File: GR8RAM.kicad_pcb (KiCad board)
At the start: 4 copper layers, 107.6 x 59.8 mm, 46 parts, among them J1 AppleIIBus, J2 JTAG, U1 EPM7128SL84, U2 512Kx8 Flash, U3 4Mx4 DRAM, U4 4Mx4 DRAM, U5 4Mx4 DRAM, U6 4Mx4 DRAM

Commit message: Board done?
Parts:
- removed JP1: Mode, Connector_PinHeader_2.54mm:PinHeader_1x02_P2.54mm_Vertical_SMD_Pin1Left
- added C23: 2u2, stdpads:C_0603, F.Cu at (103.8, 104.3)
- added C24: 2u2, stdpads:C_0603, F.Cu at (103.8, 100.9)
- added C25: 2u2, stdpads:C_0603, F.Cu at (97.2, 91.7)
- added C26: 2u2, stdpads:C_0603, F.Cu at (90.2, 91.7)
- added C27: 2u2, stdpads:C_0603, F.Cu at (106.0, 98.8)
- added C28: 2u2, stdpads:C_0603, F.Cu at (123.7, 115.3)
- added C29: 2u2, stdpads:C_0603, F.Cu at (126.5, 112.6)
- added C30: 2u2, stdpads:C_0603, F.Cu at (126.5, 107.8)
- added C31: 2u2, stdpads:C_0603, F.Cu at (126.5, 103.8)
- added C32: 2u2, stdpads:C_0603, F.Cu at (126.5, 93.4)
- added C33: 2u2, stdpads:C_0603, F.Cu at (110.8, 104.0)
- added C34: 2u2, stdpads:C_0603, F.Cu at (110.8, 108.7)
- added C35: 2u2, stdpads:C_0603, F.Cu at (113.7, 115.3)
- added C36: 10u, stdpads:C_0805, F.Cu at (131.7, 98.5)
- added C37: 10u, stdpads:C_0805, F.Cu at (131.7, 101.0)
- added C38: 22n, stdpads:R_0805, F.Cu at (129.5, 110.8)
- added D1: SS14, stdpads:D_SMA, F.Cu at (141.9, 100.0)
- added D2: SMBJ5.0A, stdpads:D_SMB, F.Cu at (137.3, 100.0)
- added D3: SS14, stdpads:D_SMA, F.Cu at (141.9, 112.7)
- added F1: nSMD035-16V, stdpads:BelFuse_1206, F.Cu at (135.4, 93.5)
- added FB1: GZ2012D601TF, stdpads:Murata_BLM21, F.Cu at (139.5, 95.5)
- added H6: , stdpads:PasteHole_1.152mm_NPTH, F.Cu at (143.0, 127.0)
- added J3: DC in, stdpads:BOOMELE_DC-005_DC_5.5-2.0MM, F.Cu at (102.8, 86.5)
- added J4: JTAG, Connector_IDC:IDC-Header_2x05_P2.54mm_Vertical, F.Cu at (64.1, 108.2)
- added Q1: AO3401A, stdpads:SOT-23, F.Cu at (141.9, 118.2)
- added R10: 1k, stdpads:R_0805, F.Cu at (132.9, 113.2)
- added R11: 1k, stdpads:R_0805, F.Cu at (138.3, 118.1)
- added R12: 1k, stdpads:R_0805, F.Cu at (139.5, 91.5)
- added R13: 100, stdpads:R_0805, F.Cu at (139.5, 93.5)
- added R14: 0, stdpads:R_0805, F.Cu at (129.8, 119.9)
- added R6: 1k, stdpads:R_0805, F.Cu at (137.1, 111.9)
- added R7: 1k, stdpads:R_0805, F.Cu at (136.1, 123.0)
- added R8: 1M, stdpads:R_0805, F.Cu at (132.9, 111.2)
- added R9: 3k3, stdpads:R_0805, F.Cu at (138.3, 114.7)
- added RN1: 4x33, stdpads:R4_0402, F.Cu at (108.2, 95.2)
- added RN2: 4x33, stdpads:R4_0402, F.Cu at (108.5, 106.2)
- added RN3: 4x33, stdpads:R4_0402, F.Cu at (108.5, 110.7)
- added RN4: 4x10k, stdpads:R4_0402, F.Cu at (128.8, 124.0)
- added U12: 74AHCT125, stdpads:TSSOP-14_4.4x5mm_P0.65mm, F.Cu at (117.0, 122.0)
- added U13: 25M, stdpads:Crystal_SMD_3225-4Pin_3.2x2.5mm, F.Cu at (107.1, 102.5)
- added U14: 74AHCT125, stdpads:TSSOP-14_4.4x5mm_P0.65mm, F.Cu at (124.5, 122.0)
- added U16: 74LVC1G04GW, stdpads:SOT-353, F.Cu at (108.2, 98.8)
- added U7: LM393, stdpads:SOIC-8_3.9mm, F.Cu at (134.5, 118.0)
- added U8: AP2125, stdpads:SOT-23, F.Cu at (138.3, 106.5)
- added U9: 74AHC245, stdpads:TSSOP-20_4.4x6.5mm_P0.65mm, F.Cu at (99.4, 122.0)
- C1, C10, C11, C2, C3, C4, C5, C6, C7, C8: value 2u2 -> 10u
- C12, C13, C17, C18, C19, C20, C21, C22, C9: footprint stdpads:C_0805 -> stdpads:C_0603
- C14, C15, C16: value DNP -> 2u2; footprint stdpads:CP_EIA-3528 -> stdpads:C_0603
- H2, H3, H4, H5: footprint stdpads:PasteHole_1.1mm_PTH -> stdpads:PasteHole_1.152mm_NPTH
- J2: footprint stdpads:IDC_SMD_2x05_P2.54mm_Vertical -> Connector:Tag-Connect_TC2050-IDC-FP_2x05_P1.27mm_Vertical
- R1, R2: value 100 -> DNP
- R3: value 100 -> 2k7
- R4: value 15 -> 2k2
- R5: value 22k -> 1M
- U1: value EPM7128SL84 -> EPM240T100C5N; footprint stdpads:PLCC-84_SMDSocket -> stdpads:TQFP-100_14x14mm_P0.5mm
- U2: value 512Kx8 Flash -> W9825; footprint stdpads:PLCC-32_SMDSocket -> stdpads:TSOP-II-54_22.2x10.16mm_P0.8mm
- U3: value 4Mx4 DRAM -> MX29LV640EB; footprint stdpads:SOP-24-26-300mil -> stdpads:TSOP-I-48_18.4x12mm_P0.5mm
- U4, U5, U6: value 4Mx4 DRAM -> 74AHC245; footprint stdpads:SOP-24-26-300mil -> stdpads:TSSOP-20_4.4x6.5mm_P0.65mm
- moved H5 108.2 mm to (140.5, 82.4), turned to 270 degrees
- moved H4 93.0 mm to (58.3, 86.0), turned to 90 degrees
- moved J2 76.6 mm to (63.9, 119.3)
- moved C8 74.4 mm to (142.6, 106.5)
- moved C3 71.3 mm to (116.2, 128.3), turned to 0 degrees
- moved U2 68.4 mm to (118.7, 103.0), turned to 180 degrees
- moved C1 65.6 mm to (136.3, 128.3)
- moved C13 60.3 mm to (76.6, 119.8), turned to 270 degrees
- moved C7 56.8 mm to (142.6, 104.5), turned to 0 degrees
- moved C16 56.0 mm to (104.2, 119.8), turned to 270 degrees
- moved C14 54.8 mm to (85.8, 119.8), turned to 270 degrees
- moved C15 53.7 mm to (95.0, 119.8), turned to 270 degrees
- moved C10 50.8 mm to (134.8, 106.5), turned to 90 degrees
- moved H1 47.1 mm to (140.5, 129.5), turned to 0 degrees
- moved R5 46.1 mm to (132.7, 123.0), turned to 0 degrees
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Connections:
- C10 pad 1: +5V -> +3V3
- C11 pad 1: +5V -> +3V3
- C12 pad 1: +5V -> +3V3
- C13 pad 1: +5V -> +3V3
- C14 pad 1: +5V -> +3V3
- C15 pad 1: +5V -> +3V3
- C16 pad 1: +5V -> +3V3
- C17 pad 1: GND -> +5V
- C17 pad 2: -5V -> GND
- C18 pad 1: +5V -> +3V3
- C18 pad 2: -5V -> GND
- C19 pad 1: +12V -> +3V3
- C2 pad 1: +5V -> GND
- C2 pad 2: GND -> -12V
- C20 pad 1: GND -> +3V3
- C20 pad 2: -12V -> GND
- C21 pad 1: +5V -> +3V3
- C21 pad 2: +12V -> GND
- C22 pad 1: -12V -> +3V3
- C22 pad 2: -5V -> GND
- C3 pad 1: +5V -> GND
- C3 pad 2: GND -> -5V
- C4 pad 1: +5V -> +12V
- C5 pad 1: +5V -> VBUS
- C6 pad 1: +5V -> Net-(C6-Pad1)
- C7 pad 1: +5V -> Vin
- C8 pad 1: +5V -> Vin
- J1 pad 22: /DMA -> /~DMA~
- J1 pad 23: /INTin -> /INTout
- J1 pad 24: /DMAin -> /DMAout
- J2 pad 4: +5V -> +3V3
- R1 pad 1: /PHI0r -> /DMAout
- R1 pad 2: /PHI0 -> /DMAin
- R2 pad 1: /PHI1r -> /INTout
- R2 pad 2: /PHI1 -> /INTin
- R3 pad 1: /Q3r -> +5V
- R3 pad 2: /Q3 -> Net-(R3-Pad2)
- R4 pad 1: /7Mr -> +3V3
- R4 pad 2: /7M -> Net-(C38-Pad1)
- R5 pad 1: +5V -> /~RES~i
- R5 pad 2: /~MODE~ -> Net-(R3-Pad2)
- U1 pad 1: /~RES~ -> /RA9
- U1 pad 10: /A9 -> GND
- U1 pad 11: /A10 -> GND
- U1 pad 12: /A11 -> /RD6
- U1 pad 13: +5V -> +3V3
- U1 pad 14: /TDI -> /RD7
- U1 pad 15: /A12 -> /RB6
- U1 pad 16: /A13 -> /RA0
- U1 pad 17: /A14 -> /D~OE~
- U1 pad 18: /A15 -> /Ddir
- U1 pad 19: GND -> /Adir
- U1 pad 2: /PHI1r -> /RD0
- U1 pad 20: /R~W~ -> /RDMAout
- U1 pad 21: /~DEVSEL~ -> /RINTout
- U1 pad 22: /~INH~ -> /TMS
- U1 pad 23: /TMS -> /TDI
- U1 pad 24: /~IOSTRB~ -> /TCK
- U1 pad 25: /D7 -> /TDO
- U1 pad 26: +5V -> /NMI~OE~
- U1 pad 27: /D6 -> /RW~OE~
- U1 pad 28: /D5 -> /RR~W~out
- U1 pad 29: /D4 -> /IRQ~OE~
- U1 pad 3: +5V -> /RA10
- U1 pad 30: /PHI1out -> /DMA~OE~
- U1 pad 31: /C7Mout -> +3V3
- U1 pad 33: /D3 -> /INH~OE~
- U1 pad 34: /D2 -> /RA11
- U1 pad 35: /D1 -> /RA12
- U1 pad 36: /D0 -> /RA13
- U1 pad 37: Net-(U1-Pad37) -> /RA14
- U1 pad 38: +5V -> /RA15
- U1 pad 39: /~CAS~0 -> /R~IOSEL~
- U1 pad 4: /A6 -> /RD1
- U1 pad 40: /~CAS~1 -> /R~DEVSEL~
- U1 pad 41: /R~CS~ -> /RPHI1
- U1 pad 42: GND -> /R~IOSTRB~
- U1 pad 43: +5V -> /RR~W~in
- U1 pad 44: /~MODE~ -> /R~RES~
- U1 pad 45: /R~OE~ -> +3V3
- U1 pad 46: /RA9 -> GND
- U1 pad 47: GND -> /Dr1
- U1 pad 48: /RA10 -> /RINTin
- U1 pad 49: /RA3 -> /RDMAin
- U1 pad 5: /A7 -> /RD2
- U1 pad 50: /RA2 -> /Dr0
- U1 pad 51: /RA5 -> /Dr4
- U1 pad 52: /RA0 -> /Dr5
- U1 pad 53: +5V -> /Dr6
- U1 pad 54: /RA1 -> /Dr7
- U1 pad 55: /RA4 -> /Dr3
- U1 pad 56: /RA7 -> /Dr2
- U1 pad 57: /RA6 -> /SDQMH
- U1 pad 58: /RA8 -> /S~WE~
- U1 pad 59: GND -> +3V3
- U1 pad 6: /Q3r -> /RD3
- U1 pad 60: /~RAS~ -> GND
- U1 pad 61: /RD7 -> /S~CAS~
- U1 pad 62: /TCK -> /S~RAS~
- U1 pad 63: /RD5 -> +3V3
- U1 pad 64: /RD6 -> /ACLK
- U1 pad 65: /RD4 -> GND
- U1 pad 66: +5V -> /SCKE
- U1 pad 67: /R~WE~ -> /S~CS~
- U1 pad 68: /RD3 -> /RB5
- U1 pad 69: /RD2 -> /RB4
- U1 pad 7: GND -> /RD4
- U1 pad 70: /RD1 -> /RB3
- U1 pad 71: /TDO -> /RB2
- U1 pad 72: GND -> /RB1
- U1 pad 73: /RD0 -> /RB0
- U1 pad 74: /~IOSEL~ -> /RB9
- U1 pad 75: /A0 -> /SA0
- U1 pad 76: /A1 -> /SA4
- U1 pad 77: /A2 -> /SA6
- U1 pad 78: +5V -> /RB10
- U1 pad 79: /A3 -> GND
- U1 pad 8: /PHI0r -> /RD5
- U1 pad 80: /A4 -> +3V3
- U1 pad 81: /A5 -> /RB11
- U1 pad 82: GND -> /RB8
- U1 pad 83: /7Mr -> /RB7
- U1 pad 84: /7Mr -> /SA3
- U1 pad 9: /A8 -> +3V3
- U2 pad 1: /RA7 -> +3V3
- U2 pad 10: /A2 -> /SD5
- U2 pad 11: /A1 -> /SD6
- U2 pad 12: /A0 -> GND
- U2 pad 13: /RD0 -> /SD7
- U2 pad 14: /RD1 -> +3V3
- U2 pad 15: /RD2 -> /SDQML
- U2 pad 16: GND -> /S~WE~
- U2 pad 17: /RD3 -> /S~CAS~
- U2 pad 18: /RD4 -> /S~RAS~
- U2 pad 19: /RD5 -> /S~CS~
- U2 pad 2: /RA5 -> /SD0
- U2 pad 20: /RD6 -> /RB4
- U2 pad 21: /RD7 -> /RB2
- U2 pad 22: /R~CS~ -> /RB0
- U2 pad 23: /A10 -> /SA0
- U2 pad 24: /R~OE~ -> /RB11
- U2 pad 25: /RA0 -> /RB8
- U2 pad 26: /A9 -> /SA3
- U2 pad 27: /A8 -> +3V3
- U2 pad 28: /RA2 -> GND
- U2 pad 29: /RA3 -> /SA4
- U2 pad 3: /RA4 -> +3V3
- U2 pad 30: /RA6 -> /RB7
- U2 pad 31: /R~WE~ -> /SA6
- U2 pad 32: +5V -> /RB10
- U2 pad 4: /RA1 -> /SD1
- U2 pad 5: /A7 -> /SD2
- U2 pad 6: /A6 -> GND
- U2 pad 7: /A5 -> /SD3
- U2 pad 8: /A4 -> /SD4
- U2 pad 9: /A3 -> +3V3
- U3 pad 1: +5V -> /RB5
- U3 pad 10: /RA2 -> /RB10
- U3 pad 11: /RA3 -> /R~WE~
- U3 pad 12: /RA10 -> +3V3
- U3 pad 13: +5V -> /RB11
- U3 pad 14: GND -> +3V3
- U3 pad 15: /RA9 -> Net-(U3-Pad15)
- U3 pad 16: /RA8 -> /RB8
- U3 pad 17: /RA6 -> /RB7
- U3 pad 18: /RA7 -> /RA8
- U3 pad 19: /RA4 -> /RA7
- U3 pad 2: /RD1 -> /RB4
- U3 pad 21: /RA1 -> /RA5
- U3 pad 22: GND -> /RA4
- U3 pad 23: /~CAS~0 -> /RA3
- U3 pad 24: /RD2 -> /RA2
- U3 pad 25: /RD0 -> /RA1
- U3 pad 26: GND -> /R~CS~
- U3 pad 3: /RD3 -> /RB3
- U3 pad 4: /R~WE~ -> /RB2
- U3 pad 5: /~RAS~ -> /RB1
- U3 pad 6: (no net) -> /RB0
- U3 pad 8: /RA0 -> /RA9
- U3 pad 9: /RA5 -> /RB9
- U4 pad 1: +5V -> /Adir
- U4 pad 10: /RA2 -> GND
- U4 pad 11: /RA5 -> /RA7
- U4 pad 12: /RA0 -> /RA6
- U4 pad 13: +5V -> /RA5
- U4 pad 14: GND -> /RA4
- U4 pad 15: /RA1 -> /RA3
- U4 pad 16: /RA4 -> /RA2
- U4 pad 17: /RA7 -> /RA1
- U4 pad 18: /RA6 -> /RA0
- U4 pad 19: /RA8 -> /A~OE~
- U4 pad 2: /RD6 -> /A0
- U4 pad 3: /RD7 -> /A1
- U4 pad 4: /R~WE~ -> /A2
- U4 pad 5: /~RAS~ -> /A3
- U4 pad 6: (no net) -> /A4
- U4 pad 8: /RA10 -> /A6
- U4 pad 9: /RA3 -> /A7
- U5 pad 1: +5V -> +3V3
- U5 pad 10: /RA2 -> GND
- U5 pad 11: /RA3 -> /RDMAin
- U5 pad 12: /RA10 -> /RINTin
- U5 pad 13: +5V -> /RR~W~in
- U5 pad 14: GND -> /R~RES~
- U5 pad 15: /RA9 -> /R~IOSTRB~
- U5 pad 16: /RA8 -> /RPHI1
- U5 pad 17: /RA6 -> /R~DEVSEL~
- U5 pad 18: /RA7 -> /R~IOSEL~
- U5 pad 19: /RA4 -> GND
- U5 pad 2: /RD1 -> /~IOSEL~
- U5 pad 3: /RD3 -> /~DEVSEL~
- U5 pad 4: /R~WE~ -> /PHI1
- U5 pad 5: /~RAS~ -> /~IOSTRB~
- U5 pad 6: (no net) -> /~RES~
- U5 pad 8: /RA0 -> /INTin
- U5 pad 9: /RA5 -> /DMAin
- U6 pad 1: +5V -> /Ddir
- U6 pad 10: /RA2 -> GND
- U6 pad 11: /RA5 -> /RD7
- U6 pad 12: /RA0 -> /RD6
- U6 pad 13: +5V -> /RD5
- U6 pad 14: GND -> /RD4
- U6 pad 15: /RA1 -> /RD3
- U6 pad 16: /RA4 -> /RD2
- U6 pad 17: /RA7 -> /RD1
- U6 pad 18: /RA6 -> /RD0
- U6 pad 19: /RA8 -> /D~OE~
- U6 pad 2: /RD6 -> /D0
- U6 pad 3: /RD7 -> /D1
- U6 pad 4: /R~WE~ -> /D2
- U6 pad 5: /~RAS~ -> /D3
- U6 pad 6: (no net) -> /D4
- U6 pad 8: /RA10 -> /D6
- U6 pad 9: /RA3 -> /D7
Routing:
- net +3V3: track 0.00 -> 137.5 mm, vias 0 -> 102
- net /A8: track 124.0 -> 12.4 mm, vias 2 -> 1
- net /A9: track 125.5 -> 13.9 mm, vias 2 -> 1
- net /A7: track 124.6 -> 14.0 mm, vias 2 -> 1
- net /~PreBOD~: track 0.00 -> 108.3 mm, vias 0 -> 2
- net /A6: track 120.2 -> 12.5 mm, vias 2 -> 1
- net /A10: track 119.3 -> 14.3 mm, vias 2 -> 1
- net /A~OE~: track 0.00 -> 95.5 mm, vias 0 -> 2
- net /A5: track 104.7 -> 12.4 mm, vias 2 -> 1
- net /A4: track 103.6 -> 12.3 mm, vias 2 -> 1
- net /A3: track 102.8 -> 13.8 mm, vias 2 -> 1
- net /TMS: track 13.8 -> 100.7 mm, vias 2 -> 1
- net /R~WE~: track 102.0 -> 15.7 mm, vias 4 -> 0
- net /A2: track 100.5 -> 14.3 mm, vias 2 -> 1
- net /RA0: track 115.4 -> 30.0 mm, vias 0 -> 2
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- added copper zone on In2.Cu, net +3V3
- removed copper zone on In2.Cu, net +5V
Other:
- board size 107.6 x 59.8 mm -> 99.9 x 59.8 mm
- net class Default: clearance 0.1524 -> 0.15; trace_width 0.1524 -> 0.15; via_dia 0.6 -> 0.5; via_drill 0.3 -> 0.2
- rule trace_clearance: 0.1524 -> 0.15
- rule trace_min: 0.1524 -> 0.15
- rule via_min_drill: 0.3 -> 0.2
- rule via_min_size: 0.4 -> 0.5
- board text added: "+5V DC in"
- board text added: "4205A"
- board text removed: "4204A"
- board text removed: "JLCJLCJLC"
- board text removed: "ZK, GF"

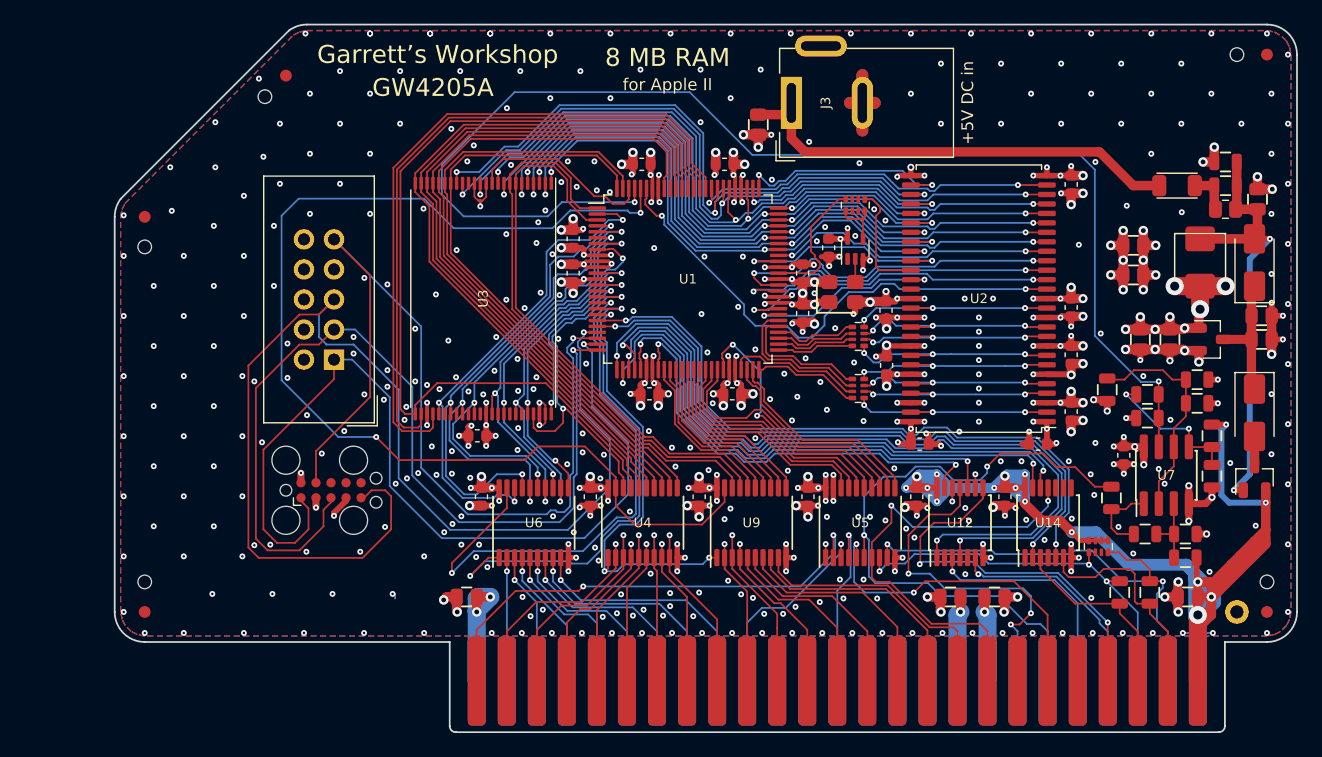
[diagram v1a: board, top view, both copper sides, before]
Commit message: reset button detect
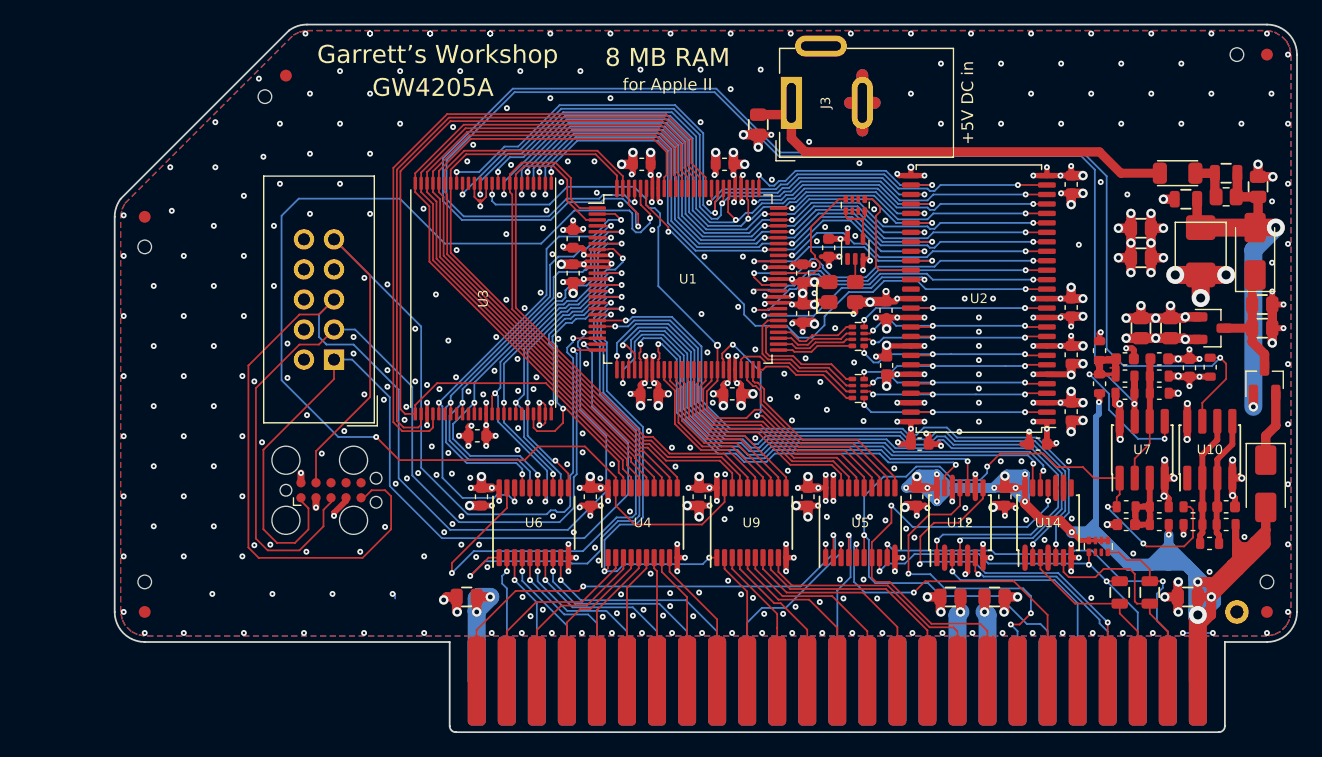
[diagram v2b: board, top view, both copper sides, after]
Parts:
- added C39: 10n, stdpads:C_0603, F.Cu at (131.1, 122.2)
- added C40: 10n, stdpads:C_0603, F.Cu at (131.0, 108.2)
- added C41: 10n, stdpads:C_0603, F.Cu at (139.6, 120.7)
- added R15: 1k, stdpads:R_0603, F.Cu at (138.2, 108.8)
- added R16: 2k2, stdpads:R_0603, F.Cu at (136.8, 120.7)
- added R17: 1k, stdpads:R_0603, F.Cu at (138.2, 123.8)
- added R18: 22k, stdpads:R_0603, F.Cu at (139.6, 122.2)
- added U10: LM393, stdpads:SOIC-8_3.9mm, F.Cu at (138.2, 115.8)
- C38: value 22n -> 10n; footprint stdpads:R_0805 -> stdpads:C_0603
- D1: value SS14 -> M7
- R10, R11, R4, R5, R6, R7, R8: footprint stdpads:R_0805 -> stdpads:R_0603
- R14: value 0 -> 1k; footprint stdpads:R_0805 -> stdpads:R_0603
- R3: value 2k7 -> 3k0; footprint stdpads:R_0805 -> stdpads:R_0603
- R9: value 3k3 -> 3k6; footprint stdpads:R_0805 -> stdpads:R_0603
- moved R11 14.2 mm to (128.8, 107.5), turned to 90 degrees
- moved R9 10.5 mm to (128.8, 110.2), turned to 90 degrees
- moved C12 9.25 mm to (136.4, 108.9), turned to 90 degrees
- moved Q1 8.29 mm to (142.8, 110.0)
- moved R14 7.26 mm to (136.8, 122.2), turned to 180 degrees
- moved D3 6.07 mm to (142.9, 118.7)
- moved C38 5.11 mm to (133.9, 108.2), turned to 0 degrees
- moved R12 4.60 mm to (136.2, 94.7)
- moved R3 3.56 mm to (133.9, 122.2)
- moved R6 3.31 mm to (133.9, 111.0)
- moved R4 3.21 mm to (133.9, 109.6)
- moved R7 3.18 mm to (133.9, 120.7)
- moved U7 2.97 mm to (132.5, 115.8)
- moved R10 2.83 mm to (131.0, 111.0)
- moved R5 2.80 mm to (131.1, 120.7)
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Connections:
- net /RDY renamed /~RDY~
- D3 pad 1: Vin -> Net-(D3-Pad1)
- D3 pad 2: Net-(D3-Pad2) -> +5V
- Q1 pad 2: +5V -> Net-(D3-Pad1)
- Q1 pad 3: Net-(D3-Pad2) -> Vin
- R14 pad 1: /~RES~ -> /M-
- R14 pad 2: /~RES~i -> GND
- R5 pad 1: /~RES~i -> /~RES~
- U1 pad 98: /R~WE~ -> /~Menu~
- U3 pad 11: /R~WE~ -> /RR~W~in
- U7 pad 1: /~RES~i -> /~RES~
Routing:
- net /~Menu~: track 0.00 -> 120.6 mm, vias 0 -> 2
- net +5V: track 166.0 -> 201.5 mm
- net /RR~W~in: track 22.1 -> 55.2 mm, vias 0 -> 2
- net GND: track 219.0 -> 236.8 mm, vias 502 -> 487
- net /~RES~: track 54.9 -> 70.8 mm, vias 2 -> 4
- net /R~WE~: track 15.7 -> 0.00 mm
- net /M-: track 0.00 -> 10.8 mm
- net /M+: track 0.00 -> 10.8 mm
- net Net-(C38-Pad1): track 18.7 -> 10.6 mm
- net /~RES~i: track 6.64 -> 0.00 mm
- net Net-(D3-Pad1): track 0.00 -> 6.05 mm
- net Net-(C40-Pad1): track 12.4 -> 17.7 mm
- net Net-(C6-Pad1): track 37.7 -> 32.6 mm
- net /A~OE~: track 95.5 -> 100.3 mm
- net /RD1: track 39.1 -> 36.3 mm
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- added copper zone on F.Cu, net Net-(C39-Pad1)
- added copper zone on F.Cu, net Net-(C40-Pad1)

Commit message: Fabbed
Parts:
- removed C17: 2u2, stdpads:C_0603
- added C42: 2u2, stdpads:C_0603, F.Cu at (116.0, 118.5)
- added C43: 2u2, stdpads:C_0603, F.Cu at (121.6, 118.5)
- added C44: 2u2, stdpads:C_0603, F.Cu at (127.2, 118.5)
- added J5: JTAG, Connector:Tag-Connect_TC2050-IDC-FP_2x05_P1.27mm_Vertical, B.Cu at (63.9, 119.3)
- added R19: 1k, stdpads:R_0603, F.Cu at (72.0, 90.8)
- added R20: 33, stdpads:R_0603, F.Cu at (125.2, 124.2)
- added R21: 33, stdpads:R_0603, F.Cu at (128.0, 124.2)
- added R22: 33, stdpads:R_0603, F.Cu at (116.8, 124.2)
- added R23: 33, stdpads:R_0603, F.Cu at (126.7, 129.8)
- added R24: 33, stdpads:R_0603, F.Cu at (122.4, 124.2)
- added R25: 33, stdpads:R_0603, F.Cu at (132.4, 129.8)
- added R26: 33, stdpads:R_0603, F.Cu at (129.6, 129.8)
- added R27: 33, stdpads:R_0603, F.Cu at (119.6, 124.2)
- added R28: 22k, stdpads:R_0603, F.Cu at (70.5, 110.7)
- added R29: 22k, stdpads:R_0603, F.Cu at (70.5, 112.1)
- added R30: 1M, stdpads:R_0603, F.Cu at (139.3, 111.0)
- added R31: 33, stdpads:R_0603, F.Cu at (81.0, 108.5)
- added RN5: 4x10k, stdpads:R4_0402, F.Cu at (69.2, 96.5)
- added U11: 74LVC1G125GW, stdpads:SOT-353, F.Cu at (125.0, 121.8)
- added U15: 74LVC1G125GW, stdpads:SOT-353, F.Cu at (126.5, 127.5)
- added U17: 74LVC1G125GW, stdpads:SOT-353, F.Cu at (122.2, 121.8)
- added U18: 74LVC1G125GW, stdpads:SOT-353, F.Cu at (132.2, 127.5)
- added U19: 74LVC1G125GW, stdpads:SOT-353, F.Cu at (129.4, 127.5)
- added U20: 74LVC1G125GW, stdpads:SOT-353, F.Cu at (113.8, 121.8)
- added U22: 74LVC1G125GW, stdpads:SOT-353, F.Cu at (119.5, 121.8)
- C38: renamed from C39; value 10n -> 22n
- C39: renamed from C38; value 10n -> 1n
- C40, C41: value 10n -> 22n
- D1: value M7 -> SS14
- F1: value nSMD035-16V -> nSMD050-16V
- FB1: value GZ2012D601TF -> GZ2012D101TF
- R1: value DNP -> 33; footprint stdpads:R_0805 -> stdpads:R_0603
- R10, R15: value 1k -> 2k2
- R11: value 1k -> 330
- R13: value 100 -> DNP
- R2: value DNP -> 2k2; footprint stdpads:R_0805 -> stdpads:R_0603
- R3: value 3k0 -> 2k7
- R7: value 1k -> 820
- R9: value 3k6 -> 1k2
- U10, U7: value LM393 -> LM393D
- U12, U14: value 74AHCT125 -> 74LVC1G125GW; footprint stdpads:TSSOP-14_4.4x5mm_P0.65mm -> stdpads:SOT-353
- U16: value 74LVC1G04GW -> 74LVC1G125GW
- U3: value MX29LV640EB -> W25Q128JVSIQ; footprint stdpads:TSOP-I-48_18.4x12mm_P0.5mm -> stdpads:SOIC-8_5.3mm
- U4, U5, U6, U9: value 74AHC245 -> 74AHC245PW
- U8: value AP2125 -> XC6206P332MR
- moved R1 19.4 mm to (114.0, 124.2), turned to 180 degrees
- moved RN4 16.7 mm to (113.5, 117.2)
- moved R2 14.3 mm to (128.9, 113.7), turned to 270 degrees
- moved C18 12.9 mm to (82.8, 103.6), turned to 90 degrees
- moved U12 10.8 mm to (127.8, 121.8), turned to 90 degrees
- moved U14 7.85 mm to (116.7, 121.8), turned to 90 degrees
- moved U3 3.33 mm to (79.1, 100.7)
- moved C9 3.19 mm to (118.7, 117.5)
- moved H3 2.54 mm to (48.1, 96.1)
- moved FID2 2.54 mm to (48.1, 93.6)
- moved FID3 1.80 mm to (58.8, 82.9)
- moved H4 1.80 mm to (57.0, 84.7)
- turned C41 to 0 degrees
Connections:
- net /DET renamed Net-(J3-Pad3)
- net /RPHI1 renamed /RPHI0
- C41 pad 1: GND -> /M+
- C41 pad 2: /M+ -> GND
- R1 pad 1: /DMAout -> /R~W~
- R1 pad 2: /DMAin -> Net-(R1-Pad2)
- R2 pad 1: /INTout -> +3V3
- R2 pad 2: /INTin -> /~BOD~
- R5 pad 1: /~RES~ -> /~BOD~
- RN4 pad 1: /INTin -> /DMAin
- RN4 pad 4: /DMAin -> /INTin
- U1 pad 1: /RA9 -> /RA4
- U1 pad 100: /RA8 -> /RA0
- U1 pad 12: /RD6 -> /FCK
- U1 pad 14: /RD7 -> /RA10
- U1 pad 15: /RB6 -> /MOSI
- U1 pad 16: /RA0 -> /MISO
- U1 pad 17: /D~OE~ -> /Ddir
- U1 pad 18: /Ddir -> /RDMAout
- U1 pad 2: /RD0 -> /RA5
- U1 pad 20: /RDMAout -> /RINTout
- U1 pad 21: /RINTout -> /DMA~OE~
- U1 pad 27: /RW~OE~ -> /INH~OE~
- U1 pad 28: /RR~W~out -> /RDY~OE~
- U1 pad 3: /RA10 -> /RA6
- U1 pad 30: /DMA~OE~ -> /RES~OE~
- U1 pad 33: /INH~OE~ -> /RR~W~out
- U1 pad 4: /RD1 -> /RA3
- U1 pad 48: /RINTin -> /RDMAin
- U1 pad 49: /RDMAin -> /RINTin
- U1 pad 5: /RD2 -> /F~CS~
- U1 pad 6: /RD3 -> /RA7
- U1 pad 68: /RB5 -> /SA12
- U1 pad 69: /RB4 -> /SBA0
- U1 pad 7: /RD4 -> /RA8
- U1 pad 70: /RB3 -> /SA11
- U1 pad 71: /RB2 -> /SBA1
- U1 pad 72: /RB1 -> /SA9
- U1 pad 73: /RB0 -> /SA10
- U1 pad 74: /RB9 -> /SA8
- U1 pad 78: /RB10 -> /SA7
- U1 pad 8: /RD5 -> /RA9
- U1 pad 81: /RB11 -> /SA1
- U1 pad 82: /RB8 -> /SA2
- U1 pad 83: /RB7 -> /SA5
- U1 pad 85: /R~OE~ -> /SDQML
- U1 pad 86: /R~CS~ -> /RD0
- U1 pad 87: /RA1 -> /RD1
- U1 pad 88: /RA2 -> /RD2
- U1 pad 89: /RA3 -> /RD3
- U1 pad 90: /RA4 -> /RD4
- U1 pad 91: /RA5 -> /RD5
- U1 pad 92: /RA6 -> /RD6
- U1 pad 95: /SDQML -> /~BOD~
- U1 pad 96: /A~OE~ -> /~PreBOD~
- U1 pad 97: /~PreBOD~ -> /RA2
- U1 pad 98: /~Menu~ -> /RA1
- U1 pad 99: /RA7 -> /RD7
- U12 pad 1: /IRQ~OE~ -> /NMI~OE~
- U12 pad 3: /~IRQ~ -> GND
- U12 pad 4: /NMI~OE~ -> Net-(R21-Pad2)
- U12 pad 5: GND -> +3V3
- U14 pad 1: GND -> /RES~OE~
- U14 pad 2: /RINTout -> GND
- U14 pad 3: /INTout -> GND
- U14 pad 4: GND -> Net-(R22-Pad2)
- U14 pad 5: /RDMAout -> +3V3
- U16 pad 1: Net-(U16-Pad1) -> GND
- U2 pad 20: /RB4 -> /SBA0
- U2 pad 21: /RB2 -> /SBA1
- U2 pad 22: /RB0 -> /SA10
- U2 pad 24: /RB11 -> /SA1
- U2 pad 25: /RB8 -> /SA2
- U2 pad 30: /RB7 -> /SA5
- U2 pad 32: /RB10 -> /SA7
- U2 pad 33: /RB9 -> /SA8
- U2 pad 34: /RB1 -> /SA9
- U2 pad 35: /RB3 -> /SA11
- U2 pad 36: /RB5 -> /SA12
- U3 pad 1: /RB5 -> /F~CS~
- U3 pad 2: /RB4 -> /MISO
- U3 pad 3: /RB3 -> /FD2
- U3 pad 4: /RB2 -> GND
- U3 pad 5: /RB1 -> /MOSI
- U3 pad 6: /RB0 -> /FCK
- U3 pad 7: /RA10 -> /FD3
- U3 pad 8: /RA9 -> +3V3
- U4 pad 19: /A~OE~ -> GND
- U5 pad 11: /RDMAin -> /RINTin
- U5 pad 12: /RINTin -> /RDMAin
- U5 pad 4: /PHI1 -> /PHI0
- U5 pad 8: /INTin -> /DMAin
- U5 pad 9: /DMAin -> /INTin
- U6 pad 19: /D~OE~ -> GND
- U7 pad 1: /~RES~ -> /~BOD~
- U9 pad 19: /A~OE~ -> GND
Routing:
- net /A~OE~: track 100.3 -> 0.00 mm, vias 2 -> 0
- net /MOSI: track 0.00 -> 97.8 mm, vias 0 -> 2
- net Net-(J5-Pad6): track 0.00 -> 96.5 mm, vias 0 -> 1
- net /~BOD~: track 0.00 -> 77.2 mm, vias 0 -> 2
- net /MISO: track 0.00 -> 73.2 mm, vias 0 -> 1
- net /F~CS~: track 0.00 -> 65.8 mm, vias 0 -> 3
- net /RB11: track 64.9 -> 0.00 mm, vias 3 -> 0
- net /RB8: track 64.8 -> 0.00 mm, vias 3 -> 0
- net /RB0: track 59.8 -> 0.00 mm, vias 3 -> 0
- net /R~OE~: track 59.0 -> 0.00 mm
- net /RB2: track 58.7 -> 0.00 mm, vias 3 -> 0
- net /RB4: track 57.6 -> 0.00 mm, vias 3 -> 0
- net /R~CS~: track 56.2 -> 0.00 mm
- net /RB7: track 55.8 -> 0.00 mm, vias 3 -> 0
- net /FD3: track 0.00 -> 54.6 mm, vias 0 -> 2
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- added copper zone on F.Cu, net Net-(C39-Pad1)
- removed copper zone on F.Cu, net Net-(C38-Pad1)
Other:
- outline, holes or cut-outs redrawn
- board text removed: "+5V DC in"
